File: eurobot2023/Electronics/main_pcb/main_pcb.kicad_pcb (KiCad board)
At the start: 2 copper layers, 120.9 x 93.2 mm, 34 parts, among them IC1 CD74HCT125M96, IC2 SN74LVC126ADR, J1 PI40HAT, J10 Conn_01x02_Male, J11 MagneticEncoder, J12 Conn_01x07_Male, J13 MagneticEncoder, J14 Conn_01x03_Male, J15 Conn_01x02_Male, J2 Conn_01x02_Male, J3 Conn_01x02_Male, J4 Conn_01x02_Male, J5 Conn_01x02_Male, J6 Conn_01x02_Male, J7 Conn_01x02_Male, J9 22-03-5035, P1 R-78Bxx-2.0, P2 Amazon 5A stepdown, U1 MCP2515-xSO, U2 TJA1049T, U3 PCA9306D, U4 Pololu_MAX14870, U5 PCA9685PW

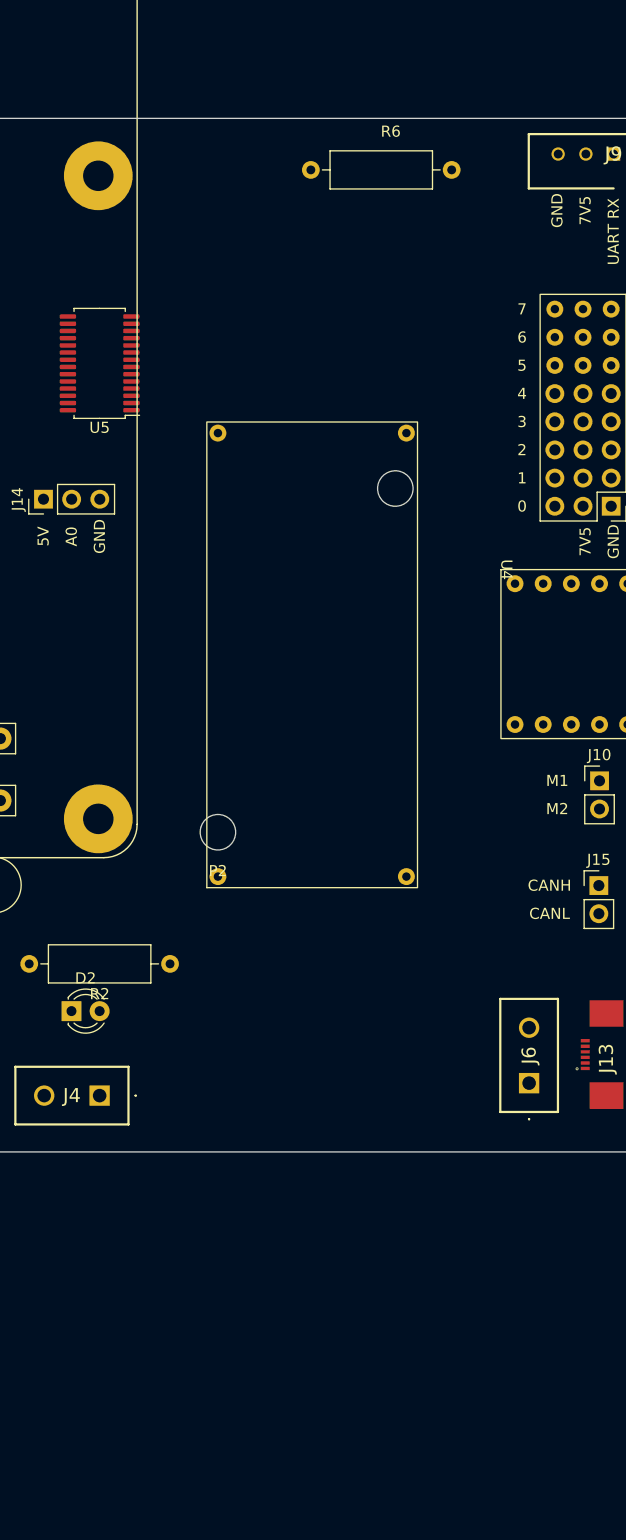
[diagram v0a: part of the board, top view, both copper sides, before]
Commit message: Electronics: fixup to SecondaryPCB and update MainPCB schematic.
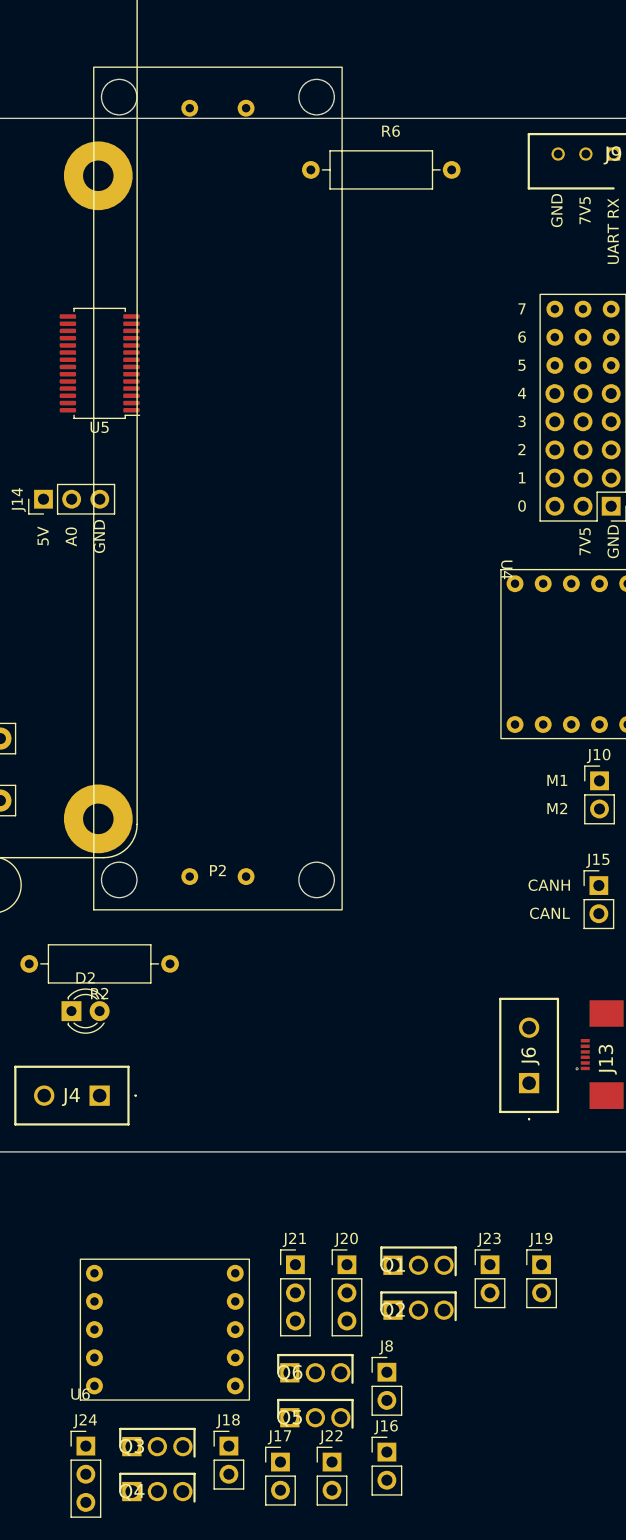
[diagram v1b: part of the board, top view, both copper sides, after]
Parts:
- added J16: Conn_01x02_Male, Connector_PinHeader_2.54mm:PinHeader_1x02_P2.54mm_Vertical, F.Cu at (160.5, 176.1)
- added J17: Conn_01x02_Male, Connector_PinHeader_2.54mm:PinHeader_1x02_P2.54mm_Vertical, F.Cu at (150.9, 177.0)
- added J18: Conn_01x02_Male, Connector_PinHeader_2.54mm:PinHeader_1x02_P2.54mm_Vertical, F.Cu at (146.3, 175.6)
- added J19: Conn_01x02_Male, Connector_PinHeader_2.54mm:PinHeader_1x02_P2.54mm_Vertical, F.Cu at (174.5, 159.2)
- added J20: Conn_01x03_Male, Connector_PinHeader_2.54mm:PinHeader_1x03_P2.54mm_Vertical, F.Cu at (156.9, 159.2)
- added J21: Conn_01x03_Male, Connector_PinHeader_2.54mm:PinHeader_1x03_P2.54mm_Vertical, F.Cu at (152.3, 159.2)
- added J22: Conn_01x02_Male, Connector_PinHeader_2.54mm:PinHeader_1x02_P2.54mm_Vertical, F.Cu at (155.6, 177.0)
- added J23: Conn_01x02_Male, Connector_PinHeader_2.54mm:PinHeader_1x02_P2.54mm_Vertical, F.Cu at (169.8, 159.2)
- added J24: Conn_01x03_Male, Connector_PinHeader_2.54mm:PinHeader_1x03_P2.54mm_Vertical, F.Cu at (133.4, 175.6)
- added J8: Conn_01x02_Male, Connector_PinHeader_2.54mm:PinHeader_1x02_P2.54mm_Vertical, F.Cu at (160.5, 168.9)
- added Q1: 2SK4017_Q_, MiAM:TO230P250X650X900-3P, F.Cu at (161.1, 159.3)
- added Q2: 2SK4017_Q_, MiAM:TO230P250X650X900-3P, F.Cu at (161.1, 163.3)
- added Q3: 2SK4017_Q_, MiAM:TO230P250X650X900-3P, F.Cu at (137.5, 175.6)
- added Q4: 2SK4017_Q_, MiAM:TO230P250X650X900-3P, F.Cu at (137.5, 179.7)
- added Q5: 2SK4017_Q_, MiAM:TO230P250X650X900-3P, F.Cu at (151.8, 173.0)
- added Q6: 2SK4017_Q_, MiAM:TO230P250X650X900-3P, F.Cu at (151.8, 169.0)
- added U6: Pololu_MAX14870, MiAM:PololuMAX14870, F.Cu at (132.9, 171.4)
- P2: value Amazon 5A stepdown -> Amazon 10A stepdown; footprint MiAM:StepDown5A -> MiAM:StepDown10A
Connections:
- J1 pad 18: unconnected-(J1-Pad18) -> /GPIO 24
- J1 pad 22: unconnected-(J1-Pad22) -> /GPIO 25
- J1 pad 33: unconnected-(J1-Pad33) -> /GPIO 13
- J1 pad 35: unconnected-(J1-Pad35) -> /GPIO 19
- J1 pad 37: unconnected-(J1-Pad37) -> /GPIO 26

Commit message: Modify pcb layout
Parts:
- moved J18 116.6 mm to (151.8, 59.1)
- moved Q3 108.8 mm to (151.6, 67.7)
- moved Q4 108.8 mm to (151.6, 71.8)
- moved J19 101.8 mm to (156.2, 59.1)
- moved J16 100.9 mm to (72.4, 127.0)
- moved J17 97.8 mm to (72.4, 118.7)
- moved Q2 93.4 mm to (78.5, 119.8), turned to 90 degrees
- moved Q1 88.1 mm to (78.5, 128.7), turned to 90 degrees
- moved J24 70.7 mm to (142.2, 105.4)
- moved J20 58.7 mm to (133.3, 105.4)
- moved J21 55.7 mm to (137.8, 105.4)
- moved U6 55.5 mm to (146.1, 117.5)
- moved J8 53.7 mm to (166.4, 115.6)
- moved Q5 47.2 mm to (146.9, 126.1)
- moved Q6 46.9 mm to (146.9, 122.3)
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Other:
- board size 120.9 x 93.2 mm -> 103.1 x 93.2 mm
- board text added: "RX"
- board text added: "SCL"
- board text added: "SDA"
- board text removed: "I2C SCL"
- board text removed: "I2C SDA"
- board text removed: "UART RX"

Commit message: Main PCB: update component placement.
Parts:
- removed J19, J22, J23: Conn_01x02_Male, Connector_PinHeader_2.54mm:PinHeader_1x02_P2.54mm_Vertical
- J16, J17, J18: value Conn_01x02_Male -> Conn_02x02_Odd_Even; footprint Connector_PinHeader_2.54mm:PinHeader_1x02_P2.54mm_Vertical -> Connector_PinHeader_2.54mm:PinHeader_2x02_P2.54mm_Vertical
- R1, R6: footprint Resistor_THT:R_Axial_DIN0309_L9.0mm_D3.2mm_P12.70mm_Horizontal -> Resistor_SMD:R_0805_2012Metric
- moved J17 93.2 mm to (144.3, 59.5), turned to -90 degrees
- moved J20 60.2 mm to (73.7, 113.0), turned to 90 degrees
- moved R6 52.4 mm to (95.1, 70.0), turned to 0 degrees
- moved J18 50.9 mm to (151.5, 110.0)
- moved R1 43.5 mm to (95.0, 115.0), turned to 180 degrees
- moved J14 39.0 mm to (128.5, 95.0), turned to 90 degrees
- moved J10 38.0 mm to (129.0, 62.0), turned to 180 degrees
- moved Q1 32.1 mm to (78.3, 96.5), turned to 180 degrees
- moved J21 30.6 mm to (144.0, 75.5)
- moved J24 20.8 mm to (139.5, 126.0), turned to 90 degrees
- moved J11 20.1 mm to (77.5, 121.0)
- moved Q2 19.4 mm to (78.3, 100.3), turned to 180 degrees
- moved J8 19.0 mm to (153.0, 102.0)
- moved J7 18.5 mm to (75.0, 128.1)
- moved J16 18.1 mm to (74.0, 109.0), turned to 90 degrees
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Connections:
- J16 pad 1: Net-(J16-Pad1) -> Net-(J20-Pad2)
- J17 pad 1: Net-(J16-Pad1) -> Net-(J21-Pad2)
- J17 pad 2: Net-(J17-Pad2) -> Net-(Q3-Pad2)
- J18 pad 1: Net-(J18-Pad1) -> Net-(J24-Pad2)
- J18 pad 2: Net-(J18-Pad2) -> Net-(Q5-Pad2)
- J20 pad 2: Net-(J16-Pad1) -> Net-(J20-Pad2)
- J21 pad 2: Net-(J18-Pad1) -> Net-(J21-Pad2)
- J24 pad 2: Net-(J22-Pad1) -> Net-(J24-Pad2)
- Q2 pad 2: Net-(J17-Pad2) -> Net-(Q2-Pad2)
- Q3 pad 2: Net-(J18-Pad2) -> Net-(Q3-Pad2)
- Q4 pad 2: Net-(J19-Pad2) -> Net-(Q4-Pad2)
- Q5 pad 2: Net-(J22-Pad2) -> Net-(Q5-Pad2)
- Q6 pad 2: Net-(J23-Pad2) -> Net-(Q6-Pad2)
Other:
- board size 103.1 x 93.2 mm -> 88 x 94 mm
- board text removed: "5V"
- board text removed: "A0"
- board text removed: "M1"
- board text removed: "M2"
- board text removed: "RX"

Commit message: Route main pcb
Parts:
- moved R2 10.2 mm to (133.3, 127.6), turned to -90 degrees
- moved J24 3.54 mm to (139.5, 129.5)
- moved C2 1.73 mm to (94.0, 83.5)
- moved Q1 1.67 mm to (76.6, 96.5)
- moved Q2 1.67 mm to (76.6, 100.3)
- moved Q6 1.35 mm to (143.0, 121.0)
- moved Q5 0.81 mm to (143.0, 117.2)
- moved R6 0.78 mm to (95.1, 69.2)
- moved U4 0.73 mm to (139.7, 82.3)
- moved R1 0.70 mm to (95.0, 114.3)
- moved J13 0.35 mm to (152.5, 120.7)
- turned D2 to 90 degrees
- turned D3 to 90 degrees
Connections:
- IC2 pad 5: /UART_RX_5 -> /UART_HD
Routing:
- net +3.3V: track 0.00 -> 222.9 mm, vias 0 -> 11
- net +7.5V: track 0.00 -> 220.7 mm, vias 0 -> 4
- net +5V: track 0.00 -> 182.4 mm, vias 0 -> 8
- net /SPI1 CLK: track 0.00 -> 162.5 mm, vias 0 -> 5
- net /SPI1_CS1: track 0.00 -> 118.9 mm, vias 0 -> 4
- net /I2C SCL: track 0.00 -> 118.3 mm, vias 0 -> 1
- net /I2C SDA: track 0.00 -> 113.7 mm, vias 0 -> 1
- net /UART_HD: track 0.00 -> 103.7 mm, vias 0 -> 4
- net +24V: track 0.00 -> 99.6 mm, vias 0 -> 2
- net /GPIO 26: track 0.00 -> 96.3 mm, vias 0 -> 2
- net Net-(J15-Pad2): track 0.00 -> 87.3 mm, vias 0 -> 2
- net Net-(J15-Pad1): track 0.00 -> 86.4 mm, vias 0 -> 2
- net Net-(J11-Pad5): track 0.00 -> 80.4 mm, vias 0 -> 2
- net /GPIO 24: track 0.00 -> 80.1 mm, vias 0 -> 2
- net /GPIO 19: track 0.00 -> 70.1 mm, vias 0 -> 2
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- added copper zone on F.Cu, net +24V
- added copper zone on B.Cu, net GND

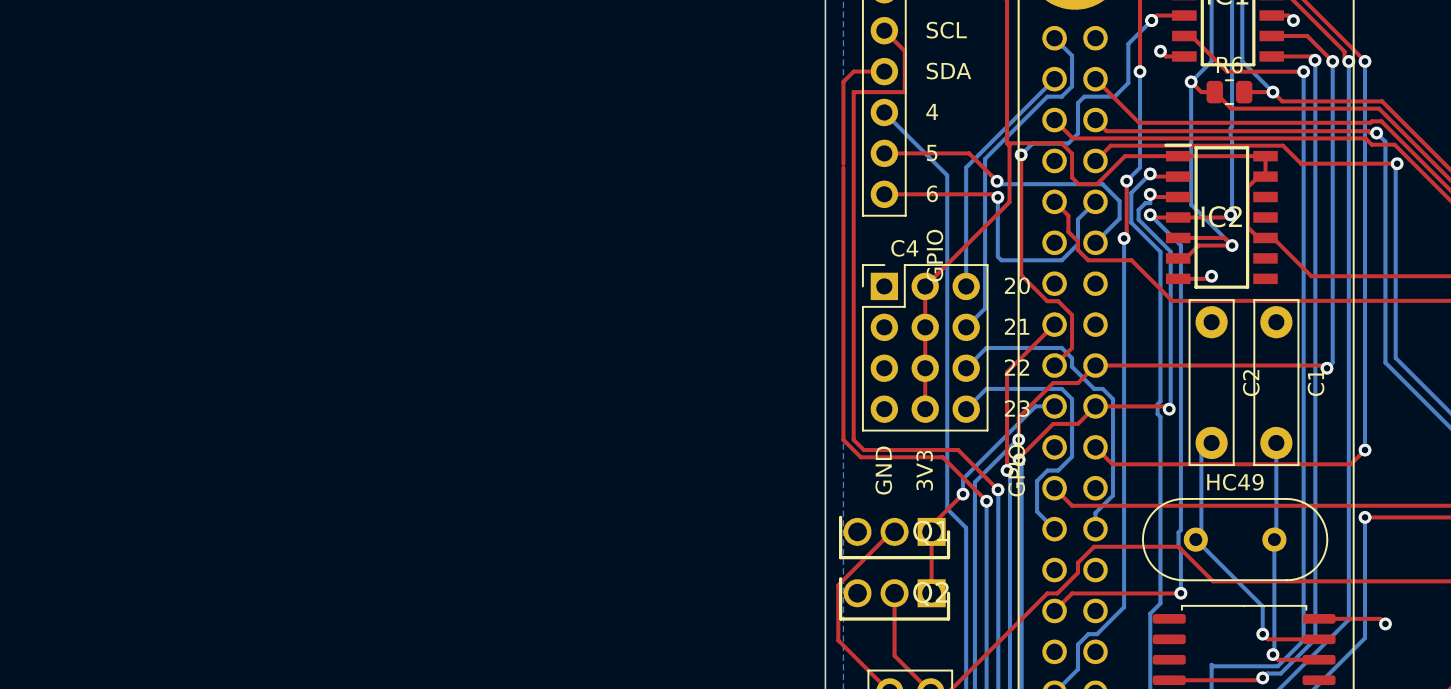
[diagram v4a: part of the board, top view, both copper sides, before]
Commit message: Electronics: correct PCB schematic and component references.
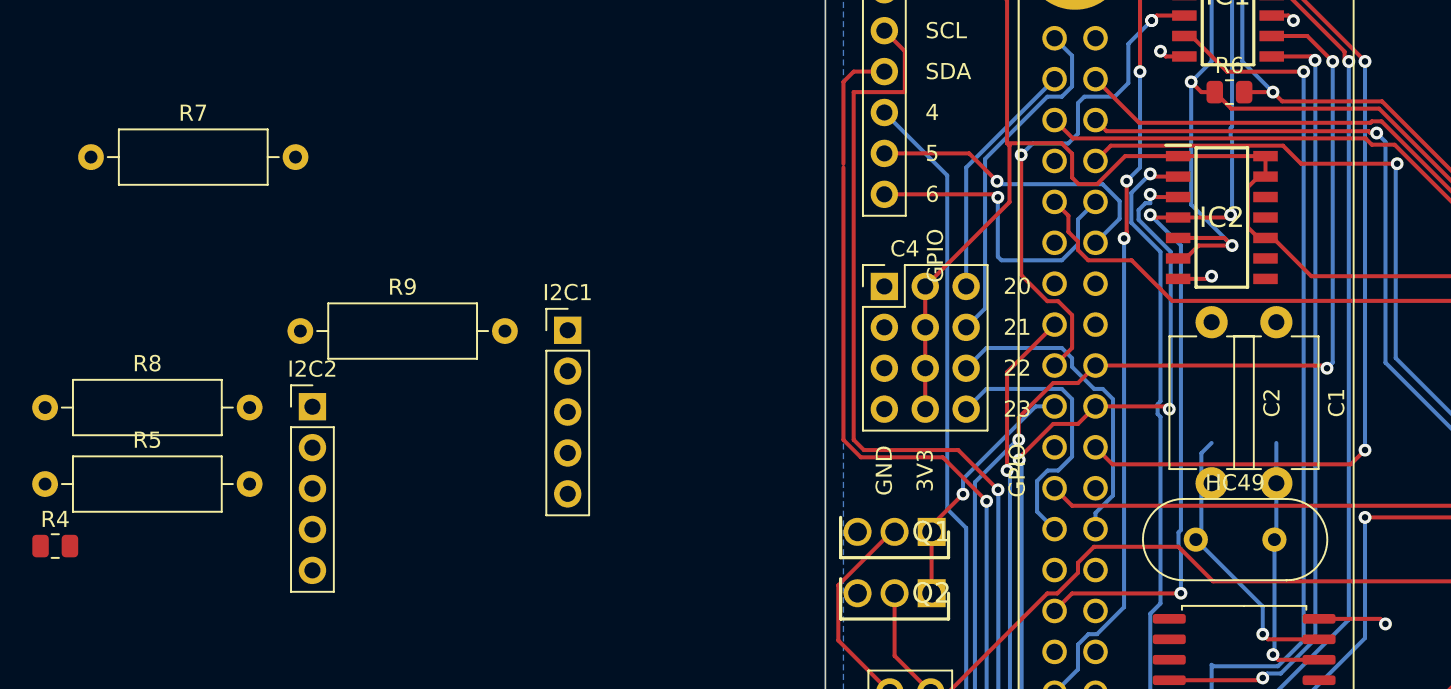
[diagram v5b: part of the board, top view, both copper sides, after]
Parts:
- added I2C1: Conn_01x05_Male, Connector_PinHeader_2.54mm:PinHeader_1x05_P2.54mm_Vertical, F.Cu at (54.0, 84.0)
- added I2C2: Conn_01x05_Male, Connector_PinHeader_2.54mm:PinHeader_1x05_P2.54mm_Vertical, F.Cu at (38.1, 88.8)
- added R4: 10k, Resistor_SMD:R_0805_2012Metric, F.Cu at (22.2, 97.4)
- added R5: 5k, Resistor_THT:R_Axial_DIN0309_L9.0mm_D3.2mm_P12.70mm_Horizontal, F.Cu at (21.6, 93.5)
- added R7: 5k, Resistor_THT:R_Axial_DIN0309_L9.0mm_D3.2mm_P12.70mm_Horizontal, F.Cu at (24.4, 73.2)
- added R8: 120, Resistor_THT:R_Axial_DIN0309_L9.0mm_D3.2mm_P12.70mm_Horizontal, F.Cu at (21.6, 88.8)
- added R9: 200k, Resistor_THT:R_Axial_DIN0309_L9.0mm_D3.2mm_P12.70mm_Horizontal, F.Cu at (37.4, 84.0)
- C1, C2: footprint Capacitor_THT:C_Rect_L10.0mm_W2.5mm_P7.50mm_MKS4 -> Capacitor_THT:C_Disc_D8.0mm_W5.0mm_P10.00mm
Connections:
- net /Servo RX renamed /Servo DIR
- IC1 pad 3: /UART_HD -> /UART_HalfDuplex
- IC2 pad 5: /UART_HD -> /UART_HalfDuplex
- IC2 pad 6: /UART_HD -> /UART_RX
- J1 pad 11: unconnected-(J1-Pad11) -> /GPIO 17
- J1 pad 13: unconnected-(J1-Pad13) -> /GPIO 27
- J9 pad 1: /UART_HD -> /UART_HalfDuplex
- R6 pad 1: /UART_HD -> /UART_HalfDuplex
- U3 pad 7: +5V -> Net-(R9-Pad1)
- U3 pad 8: unconnected-(U3-Pad8) -> Net-(R9-Pad1)
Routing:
- net /UART_HalfDuplex: track 0.00 -> 103.7 mm, vias 0 -> 4
- net /UART_HD: track 103.7 -> 0.00 mm, vias 4 -> 0
